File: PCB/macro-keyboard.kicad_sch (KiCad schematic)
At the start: 45 parts, among them J1 AVR-ISP-6, SW1 SW_Push, SW10 SW_Push, SW11 SW_Push, SW12 SW_Push, SW2 SW_Push, SW3 SW_Push, SW4 SW_Push, SW5 SW_Push, SW6 SW_Push, SW7 SW_Push, SW8 SW_Push, SW9 SW_Push, U1 PRTR5V0U2X, U2 ATmega32U4-A, Y1 Crystal_GND24_Small

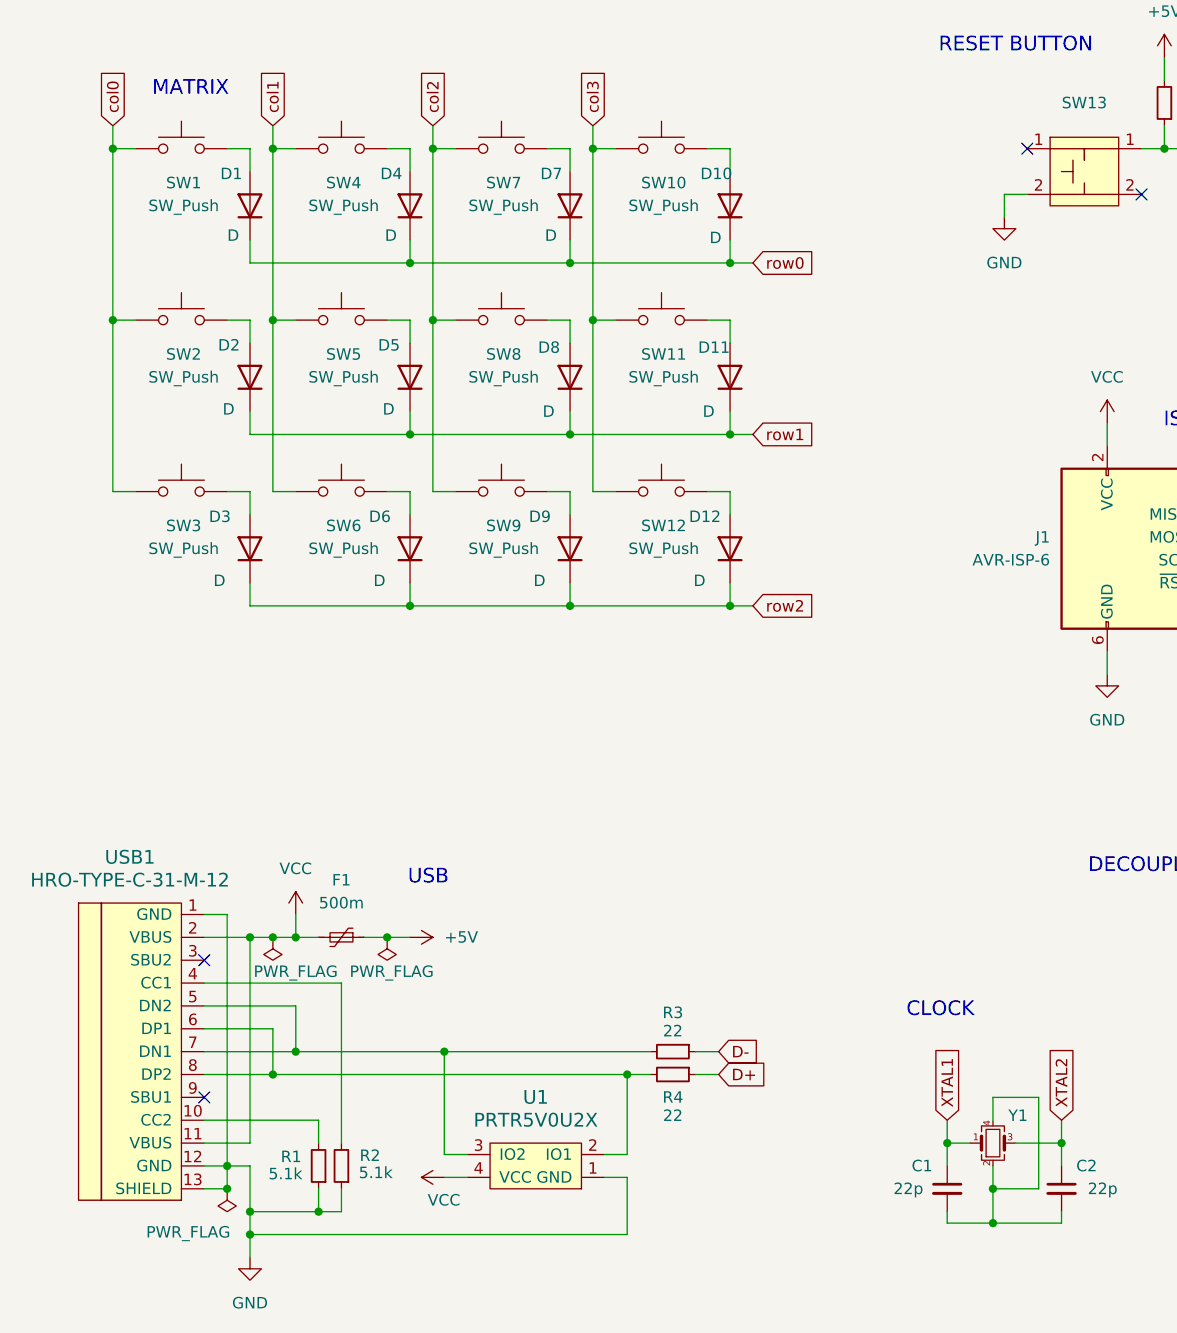
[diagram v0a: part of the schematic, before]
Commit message: Layout keycaps
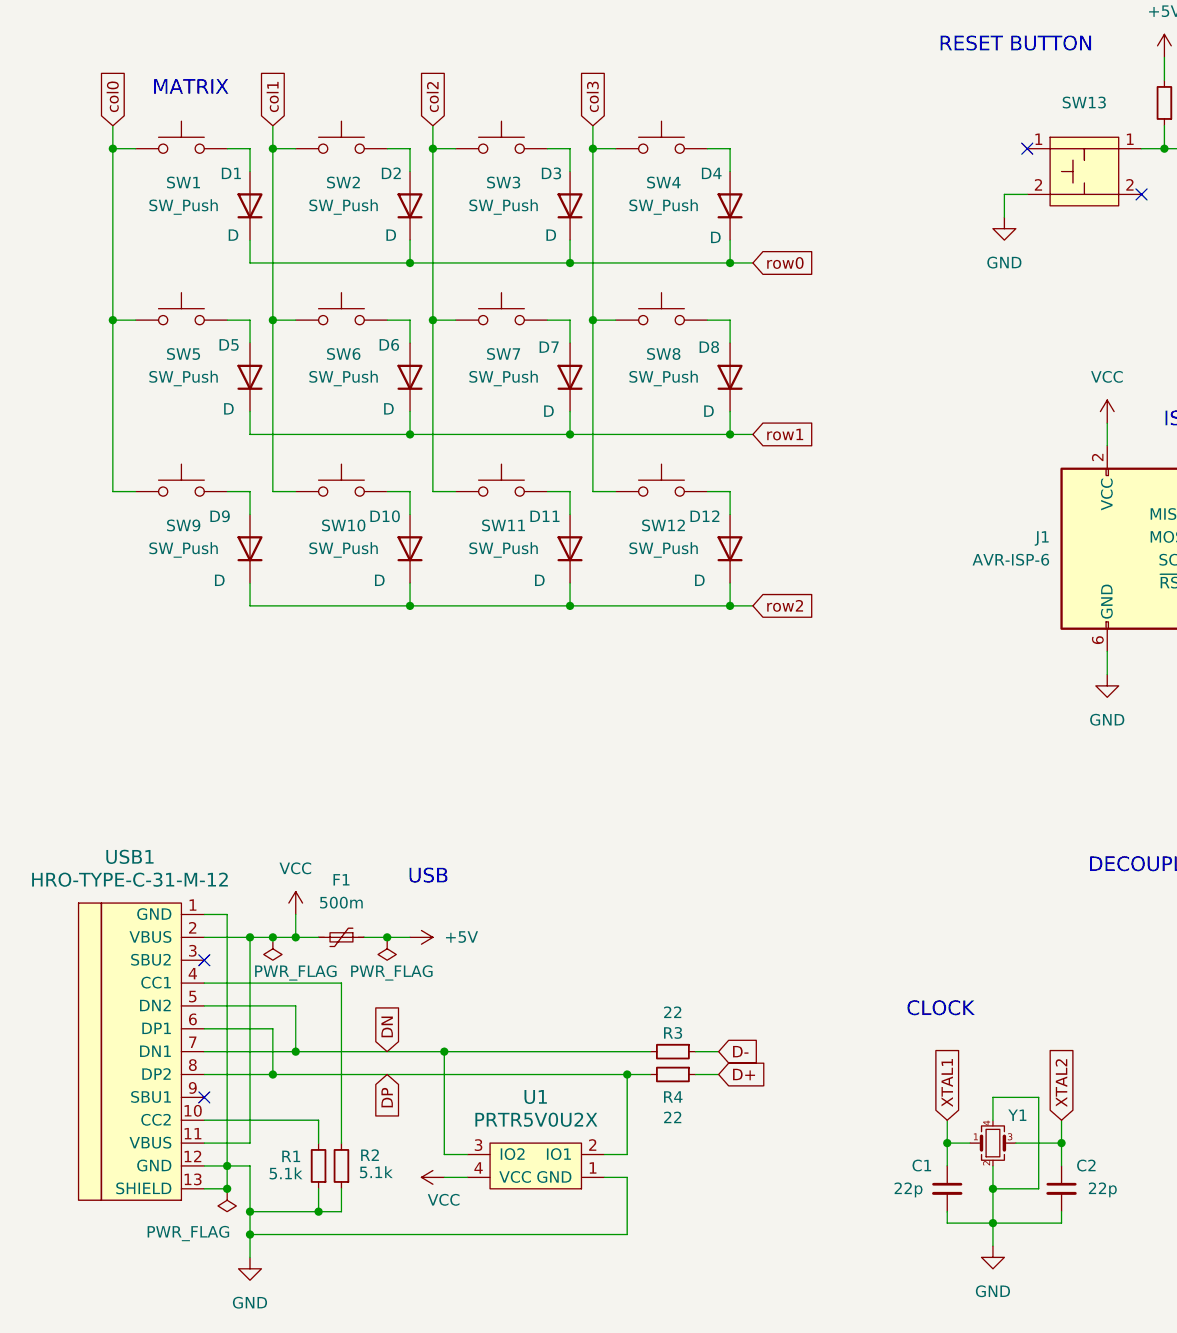
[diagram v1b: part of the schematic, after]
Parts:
- renumbered D6 to D10, D9 to D11, D4 to D2, D7 to D3, D10 to D4, D2 to D5, D5 to D6, D8 to D7, D11 to D8, D3 to D9, SW6 to SW10, SW9 to SW11, SW4 to SW2, SW7 to SW3, SW10 to SW4, SW2 to SW5, SW5 to SW6, SW8 to SW7, SW11 to SW8, SW3 to SW9
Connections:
- net GND: now also C1.2, C2.2, Y1.2, Y1.4
- net DP: now reaches R4.2, U1.2 (IO1), USB1.6 (DP1), USB1.8 (DP2)
- net DN: now reaches R3.2, U1.3 (IO2), USB1.5 (DN2), USB1.7 (DN1)

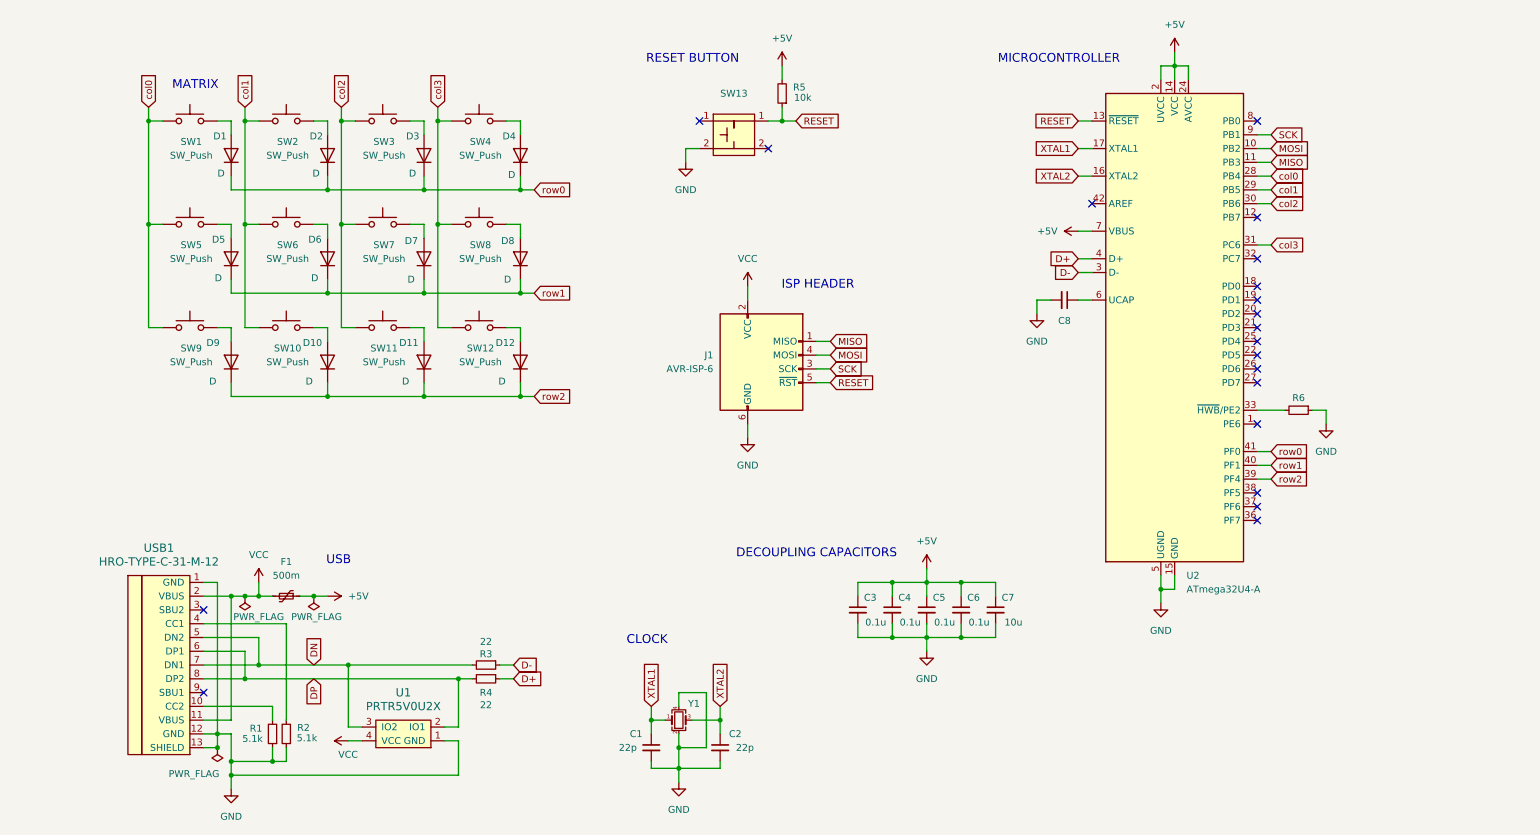
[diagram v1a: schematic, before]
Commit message: Layout traces and remove isp header and fours keys
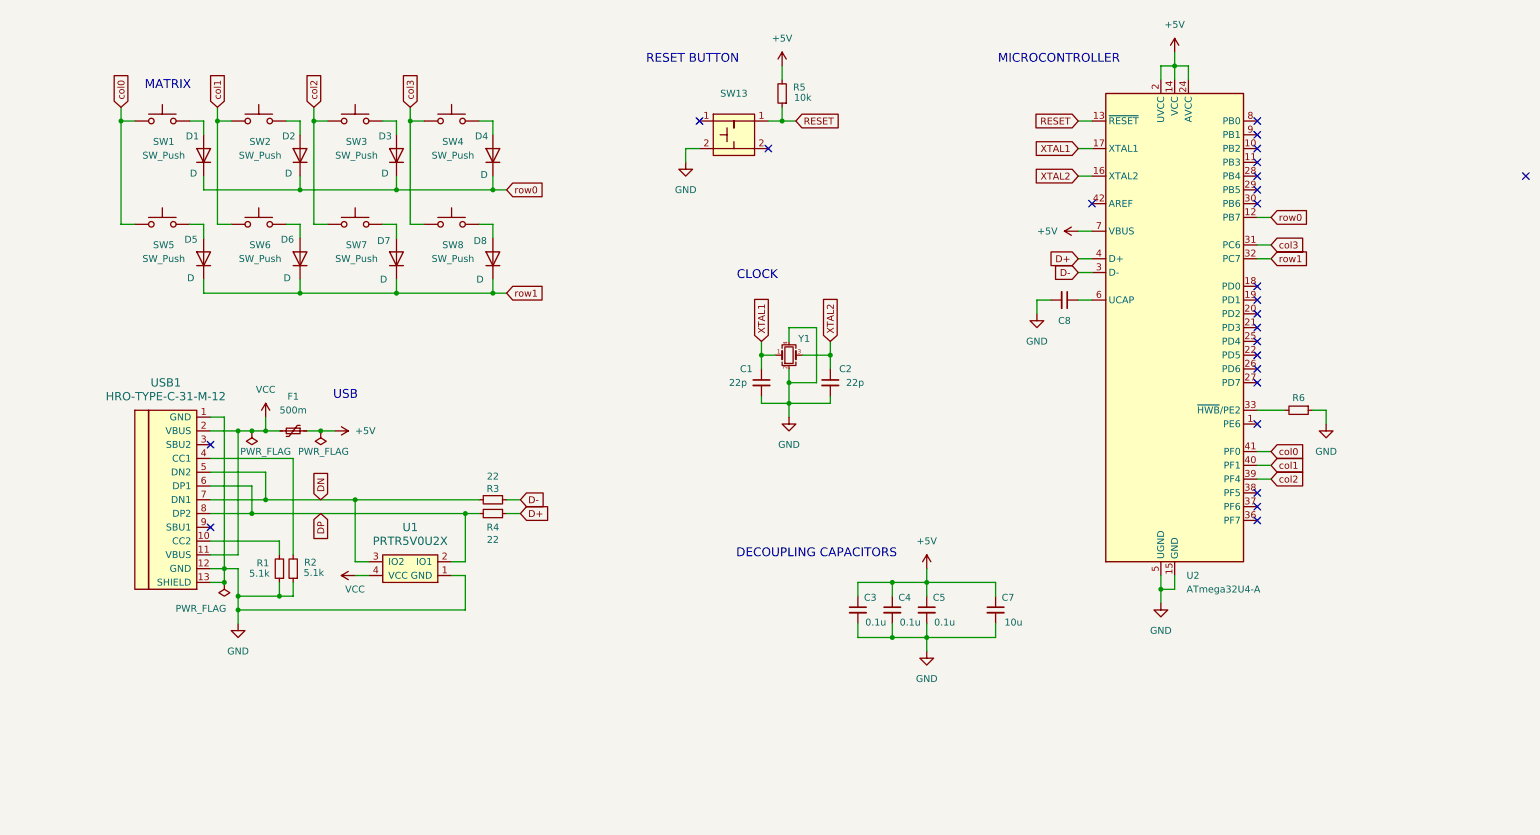
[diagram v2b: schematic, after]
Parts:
- removed C6: 0.1u, Capacitor_SMD:C_0805_2012Metric_Pad1.18x1.45mm_HandSolder, symbol Device:C_Small
- removed D10, D11, D12, D9: D, Diode_SMD:D_SOD-123, symbol Device:D
- removed J1: AVR-ISP-6, random-keyboard-parts:Reset_Pretty-Mask, symbol Connector:AVR-ISP-6
- removed SW10, SW11, SW12, SW9: SW_Push, Alps_Only:ALPS-1U, symbol Switch:SW_Push
- SW1, SW2, SW3, SW4, SW5, SW6, SW7, SW8: footprint Alps_Only:ALPS-1U -> ScottoKeebs_MX:MX_PCB_1.00u
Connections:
- net row2 is gone; now on net col2: U2.39 (PF4)
- net col0: now also U2.41 (PF0); no longer U2.28 (PB4)
- net col1: now also U2.40 (PF1); no longer U2.29 (PB5)
- net col2: no longer U2.30 (PB6)
- net row0: now also U2.12 (PB7); no longer U2.41 (PF0)
- net row1: now also U2.32 (PC7); no longer U2.40 (PF1)
- net MISO: no longer names the net of U2.11 (PB3)
- net MOSI: no longer names the net of U2.10 (PB2)
- net SCK: no longer names the net of U2.9 (PB1)
- no-connect marks 20 -> 25
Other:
- note removed: "ISP HEADER"
- moved on the sheet: C1, C2, D1, D2, D3, D4, D5, D6, D7, D8, F1, R1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

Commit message: Update models and add mounting holes
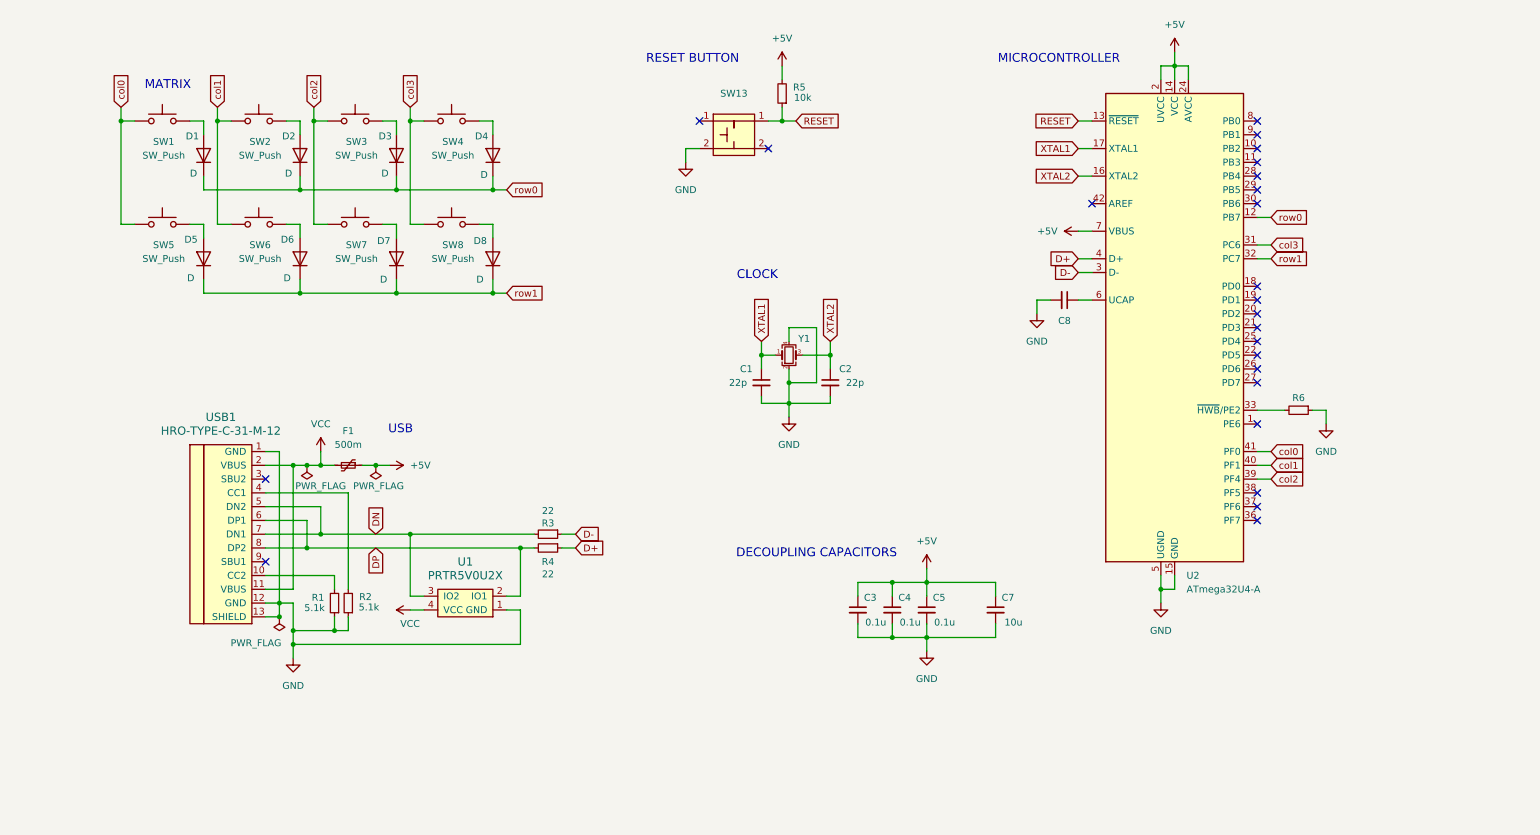
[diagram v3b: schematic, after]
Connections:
- no-connect marks 25 -> 24
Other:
- moved on the sheet: F1, R1, R2, R3, R4, U1, USB1

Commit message: Add boxes to schematic
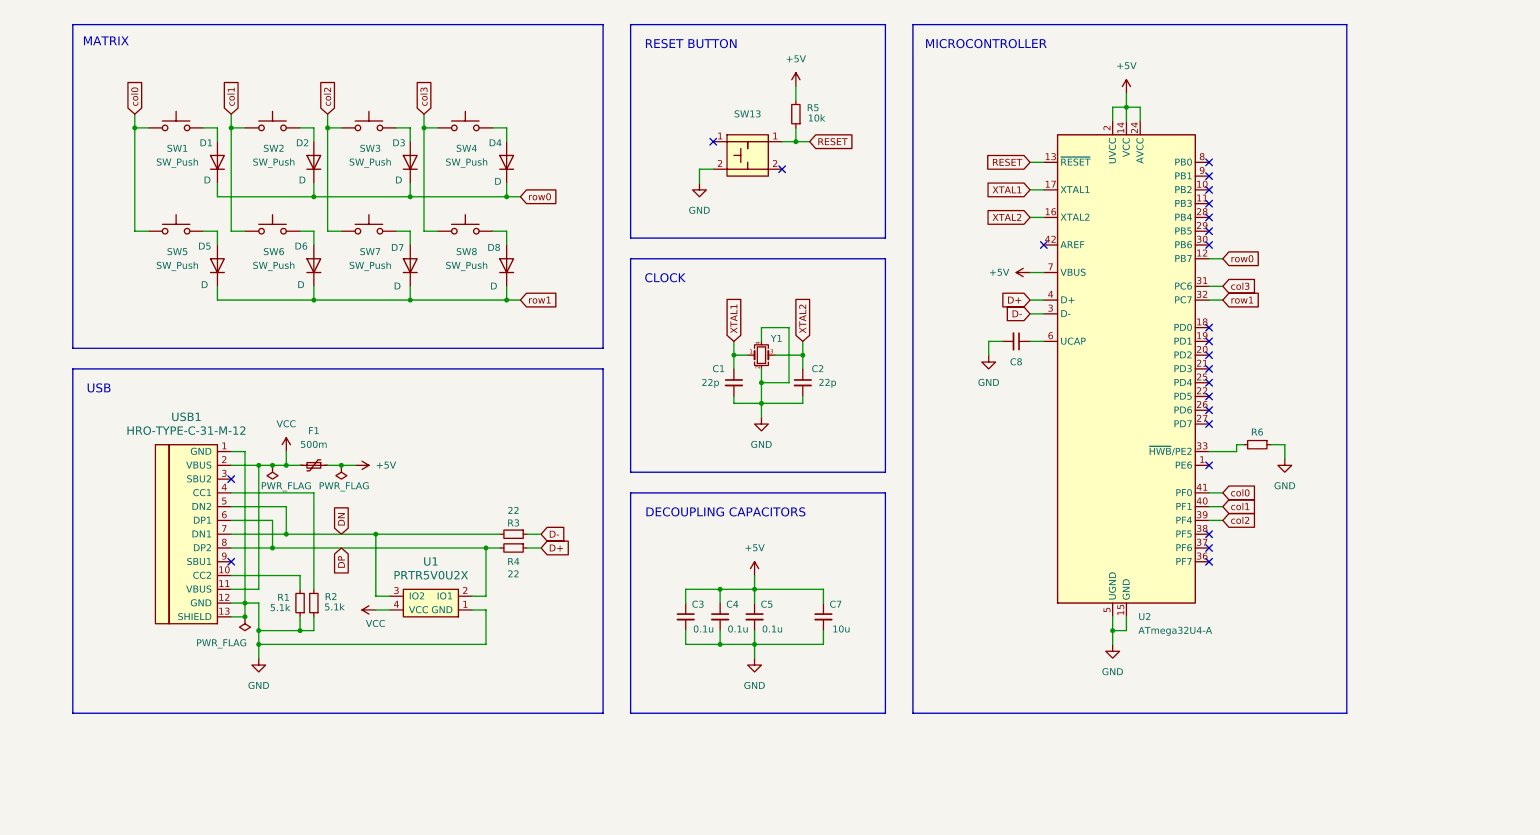
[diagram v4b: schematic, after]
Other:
- title: (none) -> Macro Keyboard 2x4
- moved on the sheet: C1, C2, C3, C4, C5, C7, C8, D1, D2, D3, D4, D5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

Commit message: Add missing decoupling capacitor
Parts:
- added C6: 0.1u, Capacitor_SMD:C_0805_2012Metric_Pad1.18x1.45mm_HandSolder, symbol Device:C_Small
- C1, C2: Part (none) -> C1804
- C3, C4, C5: Part (none) -> C62912
- C7: Part (none) -> C95841
- C8: value C_Small -> 1u; Part (none) -> C116352
- D1, D2, D3, D4, D5, D6, D7, D8: Part (none) -> C77978
- F1: Part (none) -> C70069
- R1, R2: Part (none) -> C84375
- R3, R4: Part (none) -> C150390
- R5: Part (none) -> C84376
- R6: value R_Small -> 10k; Part (none) -> C84376
- SW1, SW2, SW3, SW4, SW5, SW6, SW7, SW8: now not fitted
- SW13: Part (none) -> C221929
- U1: Part (none) -> C12333
- U2: Part (none) -> C44854
- USB1: Part (none) -> C165948
- Y1: Part (none) -> C255909
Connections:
- net +5V: now also C6.1
- net GND: now also C6.2
